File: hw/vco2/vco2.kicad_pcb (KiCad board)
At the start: 2 copper layers, 60 x 110 mm, 139 parts, among them J1 Conn_02x08_Odd_Even, Q1 DNP, U1 SSI2131, U2 TL431BCDBZ, U3 TL072HxD, U4 TL072HxD, U5 TL072HxD, U6 TL431BCDBV, U7 TL072HxD, U8 TL072HxD, U9 SSI2131

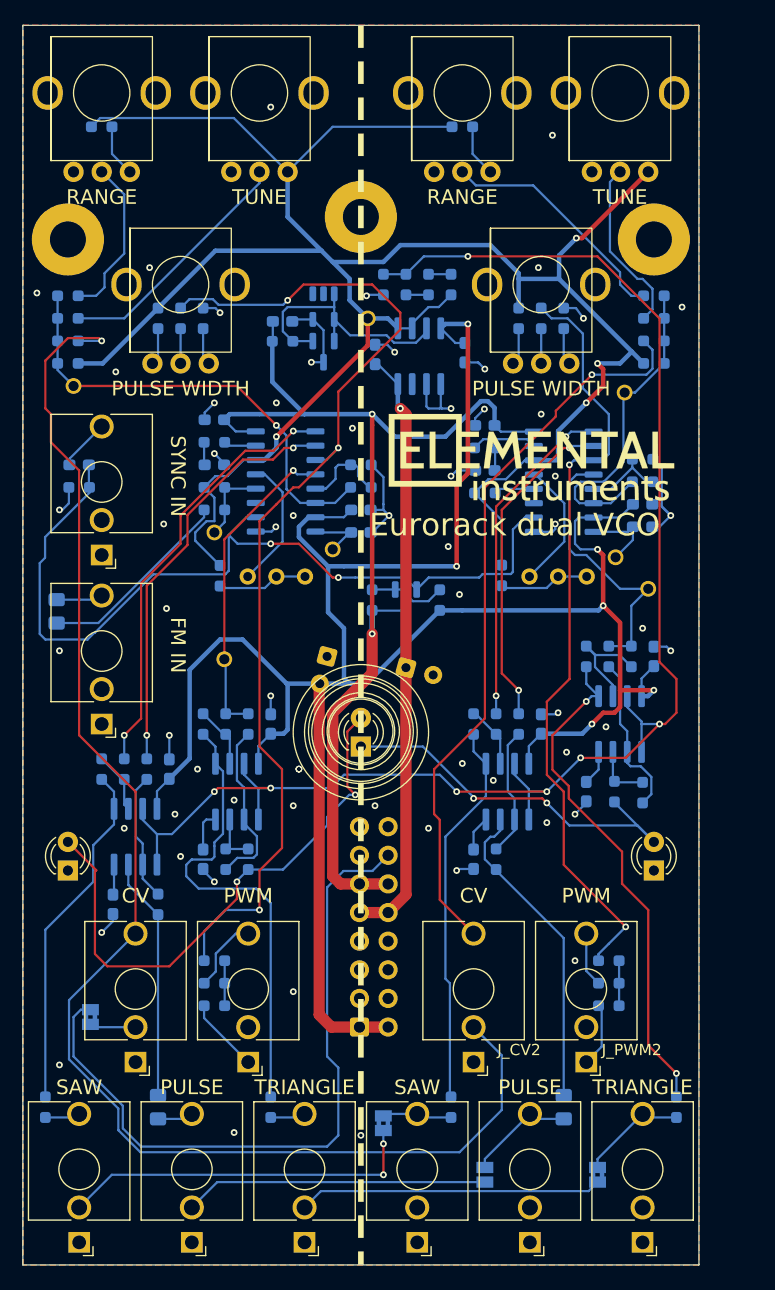
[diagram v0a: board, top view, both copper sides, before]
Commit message: WIP: Redesign VCO2 board
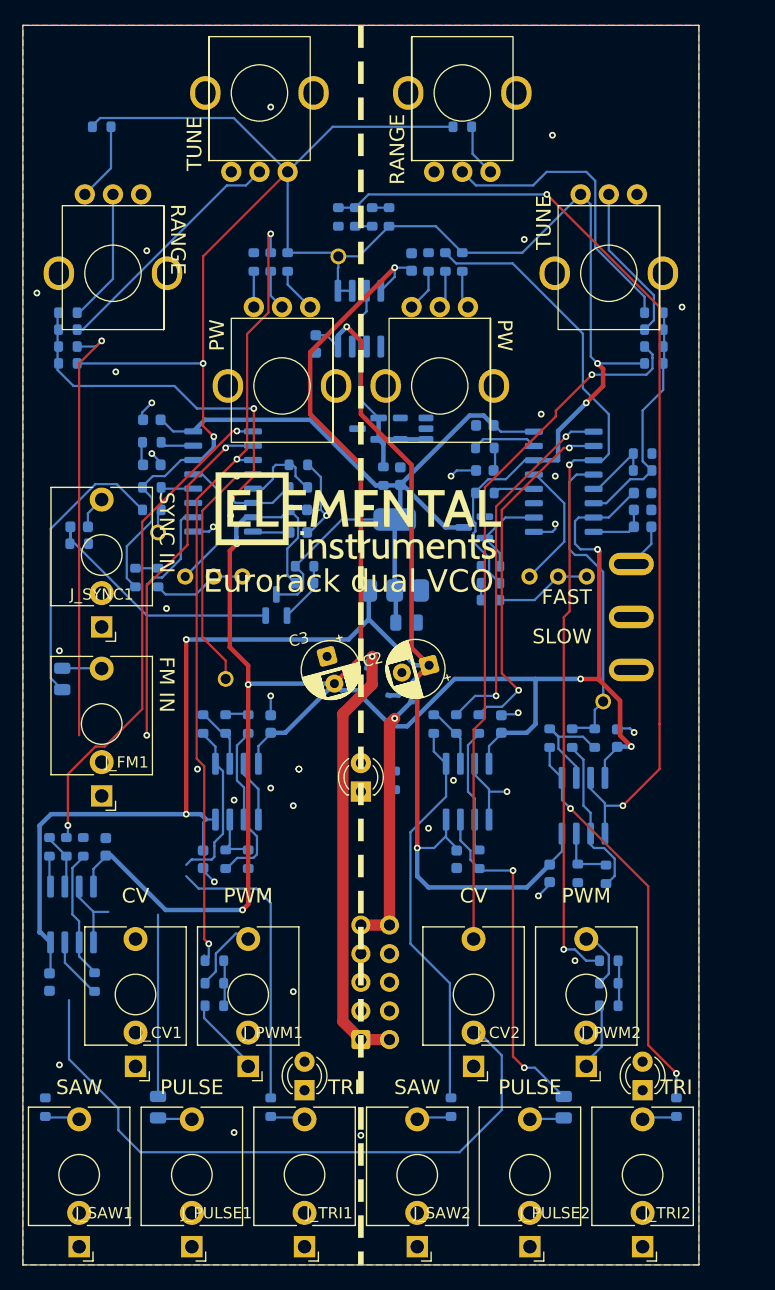
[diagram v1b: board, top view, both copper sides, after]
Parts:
- removed H1, H2, H3: MountingHole, Holes:MountingHole_3.2mm_M3_Pad
- removed JP1, JP2, JP4: jumper, Jumper:SolderJumper-2_P1.3mm_Bridged2Bar_Pad1.0x1.5mm
- removed JP3: jumper, Jumper:SolderJumper-2_P1.3mm_Open_Pad1.0x1.5mm
- removed TP10, TP2, TP6, TP7: TestPoint_Alt, Holes:TP_0.9mm
- added C17: 100n, Capacitor_SMD:C_0603_1608Metric, B.Cu at (135.0, 84.5)
- added C18: 2.2u, Capacitor_SMD:C_0805_2012Metric, B.Cu at (114.0, 93.0)
- added D4: 1N4007, Diode_SMD:D_SOD-323, B.Cu at (113.5, 99.7)
- added D5: 1N4007, Diode_SMD:D_SOD-323, B.Cu at (110.3, 98.0)
- added Q2: BC847, Package_TO_SOT_SMD:SOT-23, B.Cu at (102.5, 91.4)
- added R27: 10k, Resistor_SMD:R_0603_1608Metric, B.Cu at (121.5, 88.0)
- added R47: 10k, Resistor_SMD:R_0603_1608Metric, B.Cu at (90.0, 89.0)
- added R48: 10k, Resistor_SMD:R_0603_1608Metric, B.Cu at (121.5, 89.5)
- added R8: 1k, Resistor_SMD:R_0603_1608Metric, B.Cu at (113.0, 107.0)
- added SW1: SW_SPDT, Switch:SPDT big pads, B.Cu at (134.0, 92.5)
- added U10: TLV1117-50IDCYR, Package_TO_SOT_SMD:SOT-223-3_TabPin2, B.Cu at (113.0, 87.0)
- C1, C10, C11, C12, C13, C14, C15, C19, C20, C22, C23, C24, C25, C26, C27, C4, C5, C6, C7, C8: footprint Capacitor_SMD:C_0603_1608Metric_Pad1.08x0.95mm_HandSolder -> Capacitor_SMD:C_0603_1608Metric
- C16, C21: value 100n -> 2.2u; footprint Capacitor_SMD:C_0805_2012Metric_Pad1.18x1.45mm_HandSolder -> Capacitor_SMD:C_0805_2012Metric
- C2, C3: moved to F.Cu
- C9: footprint Capacitor_SMD:C_0805_2012Metric_Pad1.18x1.45mm_HandSolder -> Capacitor_SMD:C_0805_2012Metric
- J1: value Conn_02x08_Odd_Even -> rack_power; footprint Eurorack:IDC-Header_2x08_P2.54mm_Vertical -> Eurorack:IDC-Header_2x05_P2.54mm_Vertical
- J_CV1, J_CV2, J_FM1, J_PULSE1, J_PULSE2, J_PWM1, J_PWM2, J_SAW1, J_SAW2, J_SYNC1, J_TRI1, J_TRI2: footprint Connector_Audio:Jack_3.5mm_QingPu_WQP-PJ398SM_Vertical_CircularHoles -> Eurorack:Jack_3.5mm_PJ398SM
- Q1: value DNP -> BC847
- R1, R10, R11, R12, R14, R15, R16, R17, R18, R19, R2, R20, R21, R22, R25, R26, R28, R3, R30, R31, R32, R33, R34, R35, R37, R38, R39, R4, R41, R42, R43, R44, R45, R46, R49, R5, R50, R52, R53, R54, R55, R56, R57, R58, R59, R6, R60, R61, R62, R63, R64, R65, R67, R7, R9: footprint Resistor_SMD:R_0603_1608Metric_Pad0.98x0.95mm_HandSolder -> Resistor_SMD:R_0603_1608Metric
- R13, R66: value 20k -> 10k; footprint Resistor_SMD:R_0603_1608Metric_Pad0.98x0.95mm_HandSolder -> Resistor_SMD:R_0603_1608Metric
- R23: value DNP -> 4k3; footprint Resistor_SMD:R_0603_1608Metric_Pad0.98x0.95mm_HandSolder -> Resistor_SMD:R_0603_1608Metric
- R24: value DNP -> 10k; footprint Resistor_SMD:R_0603_1608Metric_Pad0.98x0.95mm_HandSolder -> Resistor_SMD:R_0603_1608Metric
- R29, R40: value 20k -> 4k3; footprint Resistor_SMD:R_0603_1608Metric_Pad0.98x0.95mm_HandSolder -> Resistor_SMD:R_0603_1608Metric
- R36, R51: value 32k -> 39k; footprint Resistor_SMD:R_0603_1608Metric_Pad0.98x0.95mm_HandSolder -> Resistor_SMD:R_0603_1608Metric
- moved D2 28.7 mm to (105.0, 134.5)
- moved D3 19.5 mm to (135.0, 134.5)
- moved C13 17.3 mm to (113.5, 80.0), turned to -90 degrees
- moved G*** 16.2 mm to (109.6, 83.7)
- moved RV_RANGE1 16.0 mm to (88.0, 62.0), turned to -90 degrees
- moved RV_TUNE2 16.0 mm to (132.0, 62.0), turned to -90 degrees
- moved R25 14.9 mm to (112.0, 80.0), turned to -90 degrees
- moved U6 13.4 mm to (114.6, 75.8), turned to 180 degrees
- moved R41 13.0 mm to (116.0, 61.0)
- moved RV_PWM1 12.7 mm to (103.0, 72.0), turned to -90 degrees
- moved RV_PWM2 12.7 mm to (117.0, 72.0), turned to -90 degrees
- moved R29 12.5 mm to (103.5, 61.0)
- moved R24 12.1 mm to (105.0, 89.5), turned to 180 degrees
- moved TP9 10.8 mm to (131.5, 100.0)
- moved R42 9.86 mm to (117.5, 61.0)
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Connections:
- net /Oscillator 2/TCAP renamed /TCAP2
- C10 pad 2: ANTI_HANGUP -> /HARD_SYNC1
- D2 pad 2: Net-(D1-A) -> Net-(D2-A)
- D3 pad 2: Net-(D1-K) -> Net-(D3-A)
- J1 pad 1: -12V -> Net-(D5-K)
- J1 pad 10: +12V -> Net-(D4-A)
- J1 pad 2: -12V -> Net-(D5-K)
- J1 pad 9: +12V -> Net-(D4-A)
- Q1 pad 2: ANTI_HANGUP -> /HARD_SYNC2
- R13 pad 1: +2V5 -> Net-(R13-Pad1)
- R22 pad 1: ANTI_HANGUP -> /HARD_SYNC1
- R26 pad 1: Net-(R26-Pad1) -> Net-(D1-A)
- R26 pad 2: Net-(D1-A) -> Net-(D2-A)
- R37 pad 1: Net-(R26-Pad1) -> Net-(D1-A)
- R62 pad 2: Net-(D1-K) -> Net-(D3-A)
- R66 pad 1: +2V5 -> Net-(R48-Pad2)
- U1 pad 10: ANTI_HANGUP -> /HARD_SYNC1
- U5 pad 7: Net-(R26-Pad1) -> Net-(D1-A)
- U9 pad 10: ANTI_HANGUP -> /HARD_SYNC2
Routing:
- net +12V: track 65.7 -> 158.1 mm, vias 1 -> 4
- net ANTI_HANGUP: track 76.5 -> 0.00 mm, vias 2 -> 0
- net Net-(J1-Pin_14): track 62.7 -> 0.00 mm
- net Net-(D1-A): track 49.9 -> 4.76 mm, vias 2 -> 0
- net GND: track 82.3 -> 39.3 mm, vias 62 -> 35
- net Net-(D5-K): track 0.00 -> 39.4 mm, vias 0 -> 1
- net OPREF: track 141.1 -> 105.1 mm, vias 7 -> 4
- net Net-(D1-K): track 34.6 -> 0.00 mm, vias 2 -> 0
- net /HARD_SYNC1: track 0.00 -> 34.1 mm
- net Net-(J_CV1-PadT): track 128.7 -> 96.3 mm
- net Net-(JP2-B): track 32.1 -> 0.00 mm, vias 2 -> 0
- net Net-(R2-Pad1): track 31.2 -> 2.74 mm
- net Net-(JP4-B): track 26.9 -> 0.00 mm
- net Net-(JP3-B): track 26.9 -> 0.00 mm
- net Net-(D4-A): track 0.00 -> 23.2 mm, vias 0 -> 1
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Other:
- board text added: "Dual VCO rev2"
- board text added: "FAST"
- board text added: "PW"
- board text added: "SLOW"
- board text added: "TRI"
- board text removed: "Dual VCO rev1"
- board text removed: "PULSE WIDTH"
- board text removed: "TRIANGLE"

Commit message: VCO2 production work
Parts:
- added G***: LOGO, LOGO, B.Cu at (110.5, 143.5)
- R16, R45: value 250k -> 267k
- R31, R39: value 10k -> 4k3
- RV_PWM1, RV_PWM2, RV_RANGE1, RV_RANGE2, RV_TUNE1, RV_TUNE2: value 20k -> 10k
- moved R8 4.72 mm to (110.6, 111.1), turned to 0 degrees
- moved G*** 1.49 mm to (109.6, 85.2)
- moved TP4 0.87 mm to (92.9, 85.0)
- turned Q1 to -90 degrees
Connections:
- J_CV1 pad TN: BACKPLANE_CV -> unconnected-(J_CV1-PadTN)
- J_PULSE1 pad TN: Net-(JP3-B) -> unconnected-(J_PULSE1-PadTN)
- J_SAW1 pad TN: Net-(JP2-B) -> unconnected-(J_SAW1-PadTN)
- J_TRI1 pad TN: Net-(JP4-B) -> unconnected-(J_TRI1-PadTN)
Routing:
- net OPREF: track 105.1 -> 165.9 mm
- net Net-(R59-Pad1): track 5.20 -> 29.8 mm
- net Net-(R2-Pad1): track 2.74 -> 22.1 mm, vias 0 -> 2
- net Net-(D2-A): track 0.00 -> 19.2 mm
- net Net-(D3-A): track 0.05 -> 18.3 mm
- net Net-(D1-A): track 4.76 -> 20.6 mm, vias 0 -> 2
- net Net-(Q1-B): track 5.36 -> 20.9 mm
- net /PULSE1: track 30.9 -> 46.5 mm
- net Net-(J_CV1-PadT): track 96.3 -> 106.0 mm
- net /SAW1: track 44.5 -> 50.6 mm
- net Net-(U5B--): track 15.1 -> 19.2 mm
- net /EXPO_FREQ1: track 38.0 -> 41.8 mm
- net Net-(C16-Pad1): track 21.6 -> 18.3 mm
- net /TRI1: track 23.6 -> 26.8 mm
- net Net-(D1-K): track 0.00 -> 3.16 mm
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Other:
- board text added: "-12V"
- board text added: "Flammingo drawing: https://runeberg.org/nfbh/0296.html"
- board text added: "Oscillator 1"
- board text added: "Oscillator 2"
